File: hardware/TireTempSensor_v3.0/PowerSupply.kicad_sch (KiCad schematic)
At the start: 43 parts, among them IC3 TPS54202HDDCR, IC4 TPS54202HDDCR, Q1 FQT3P20TF, T10 TP_+5V, T11 TP_+5V, T12 TP_+5V, T13 TP_+5V, T14 TP_+3.3V, T15 TP_+2.6V, T8 TP_VCC, U2 MIC5306-2.6YD5-TR

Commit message: Piotruś prosił :3
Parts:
- removed C24, C30, C31: 22u, Capacitor_SMD:C_0805_2012Metric_Pad1.18x1.45mm_HandSolder, symbol Device:C_Small
- removed C25: 100n, Capacitor_SMD:C_0603_1608Metric_Pad1.08x0.95mm_HandSolder, symbol Device:C_Small
- removed IC3: TPS54202HDDCR, Package_TO_SOT_SMD:SOT-23-6_Handsoldering, symbol SamacsysNew:TPS54202HDDCR
- removed L3: 68u/1A4, Inductor_SMD:L_TDK_VLS6045EX_VLS6045AF, symbol Samacsys_kicad_sym:SRR4028-271Y
- removed R12: 510k, Resistor_SMD:R_0603_1608Metric_Pad0.98x0.95mm_HandSolder, symbol Device:R_Small
- removed R13: 21.8k, Resistor_SMD:R_0603_1608Metric_Pad0.98x0.95mm_HandSolder, symbol Device:R_Small
- removed T11: TP_+5V, TestPoint:TestPoint_Pad_1.0x1.0mm, symbol Connector:TestPoint_Small
- removed T8: TP_VCC, TestPoint:TestPoint_Pad_1.0x1.0mm, symbol Connector:TestPoint_Small
- added C44: 10u, Capacitor_SMD:C_0603_1608Metric_Pad1.08x0.95mm_HandSolder, symbol Device:C_Small
- added C45: 22u, Capacitor_SMD:C_0805_2012Metric_Pad1.18x1.45mm_HandSolder, symbol Device:C_Small
- added D13: +3V3, LED_SMD:LED_0603_1608Metric_Pad1.05x0.95mm_HandSolder, symbol Device:LED_Small
- added U3: LM1117-3.3, Package_TO_SOT_SMD:SOT-223-3_TabPin2, symbol Regulator_Linear:LM1117MP-3.3
- C29: value 22u -> 100n; footprint Capacitor_SMD:C_0805_2012Metric_Pad1.18x1.45mm_HandSolder -> Capacitor_SMD:C_0603_1608Metric_Pad1.08x0.95mm_HandSolder; Manufacturer_Name MCASH21GCC7684MTCA1J -> (none); Manufacturer_Part_Number CL21A107MQYNNWE -> (none); Mouser Part Number 810-C2012X5R1V226MAC -> (none); Mouser Price/Stock https://www.mouser.pl/ProductDetail/TDK/C2012X5R1V226M125AC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 -> https://www.mouser.pl/ProductDetail/Murata-Electronics/GRM0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
- R14: value 100k -> 1k; Manufacturer_Name -- -> (none); Manufacturer_Part_Number RT0603DRE07100KL -> (none); Mouser Part Number 603-RT0603DRE07100KL -> (none); Mouser Price/Stock https://www.mouser.pl/ProductDetail/KOA-Speer/RK73B1JTTD104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 -> https://www.mouser.pl/ProductDetail/Vishay-Dale/CRCW06031K0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
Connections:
- net BOOT_+3.3V is gone; now on net +5V: C27.1
- net SW_+3.3V is gone; now on net GND: C27.2
- net +5V: now also C44.1, U3.3 (VI)
- net +5V_OUT: no longer C29.1, F3.2, R14.2
- net GND: now also C44.2, C45.2, D13.1 (K), U3.1 (GND)
- net FB_+3.3V renamed VO_+3.3V
- net VO_+3.3V: now also C29.1, F3.2, C45.1, U3.2 (VO)
- new net D3V3_to_R1k: D13.2 (A), R14.2
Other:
- moved on the sheet: C14, C15, F3, F4, FB2, T14, T15, U2

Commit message: Poprawki, kontynuacja layoutu
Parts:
- Q1: footprint Mosfet:SOT-223-4-NFET -> Package_TO_SOT_SMD:SOT-223-3_TabPin2
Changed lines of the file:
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@@
 			)
 		)
-		(property "Footprint" "Mosfet:SOT-223-4-NFET"
+		(property "Footprint" "Package_TO_SOT_SMD:SOT-223-3_TabPin2"
 			(at 105.41 36.83 0)
 			(effects
@@
 			)
 		)
-		(property "Datasheet" "https://www.mouser.pl/ProductDetail/onsemi-Fairchild/FQT3P20TF?qs=k6rL%2Fc%252BPp3KKqr%252BK9hIArg%3D%3D"
+		(property "Datasheet" "https://www.mouser.pl/ProductDetail/Diodes-Incorporated/ZVP2120GTA?qs=xZ%2FP%252Ba9zWqYgxv%2FYfJ%252BkQg%3D%3D"
 			(at 107.95 41.91 0)
 			(effects

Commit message: Propozycja layoutu na spotkanie
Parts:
- removed JP1: SolderJumper_2_Open, Jumper:SolderJumper-2_P1.3mm_Open_TrianglePad1.0x1.5mm, symbol Jumper:SolderJumper_2_Open
- removed Q1: FQT3P20TF, Package_TO_SOT_SMD:SOT-223-3_TabPin2, symbol Device:Q_PMOS_DSG
- added D16: D_Schottky, Diode_SMD:D_SOD-882D, symbol Device:D_Schottky
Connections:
- net +24V safe: now also D16.1 (K)
- net at F2.2: now also D16.2 (A)
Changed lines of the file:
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@@
 	)
 	(junction
-		(at 118.11 39.37)
-		(diameter 0)
-		(color 0 0 0 0)
-	)
-	(junction
 		(at 151.13 154.305)
 		(diameter 0)
@@
 	)
 	(junction
-		(at 97.79 39.37)
-		(diameter 0)
-		(color 0 0 0 0)
-	)
-	(junction
 		(at 151.13 167.005)
 		(diameter 0)
@@
 	(wire
 		(pts
-			(xy 118.11 26.67) (xy 118.11 39.37)
-		)
-		(stroke
-			(width 0)
-			(type default)
-		)
-	)
-	(wire
-		(pts
-			(xy 111.76 26.67) (xy 118.11 26.67)
-		)
-		(stroke
-			(width 0)
-			(type default)
-		)
-	)
-	(wire
-		(pts
 			(xy 116.84 154.305) (xy 123.19 154.305)
 		)
@@
 	(wire
 		(pts
-			(xy 97.79 39.37) (xy 102.87 39.37)
+			(xy 127.635 70.485) (xy 127.635 72.39)
 		)
 		(stroke
@@
 	(wire
 		(pts
-			(xy 127.635 70.485) (xy 127.635 72.39)
+			(xy 105.41 39.37) (xy 132.715 39.37)
 		)
 		(stroke
@@
 	(wire
 		(pts
-			(xy 97.79 26.67) (xy 104.14 26.67)
-		)
-		(stroke
-			(width 0)
-			(type default)
-		)
-	)
-	(wire
-		(pts
 			(xy 60.96 164.465) (xy 60.96 167.005)
 		)
@@
 	(wire
 		(pts
-			(xy 97.79 39.37) (xy 97.79 26.67)
-		)
-		(stroke
-			(width 0)
-			(type default)
-		)
-	)
-	(wire
-		(pts
 			(xy 60.96 137.795) (xy 60.96 139.065)
 		)
@@
 	(wire
 		(pts
-			(xy 118.11 39.37) (xy 132.715 39.37)
-		)
-		(stroke
-			(width 0)
-			(type default)
-		)
-	)
-	(wire
-		(pts
 			(xy 93.98 167.005) (xy 72.39 167.005)
 		)
@@
 	(wire
 		(pts
-			(xy 113.03 39.37) (xy 118.11 39.37)
-		)
-		(stroke
-			(width 0)
-			(type default)
-		)
-	)
-	(wire
-		(pts
 			(xy 252.73 55.88) (xy 252.73 58.42)
 		)
@@
 	)
 	(symbol
+		(lib_id "Device:D_Schottky")
+		(at 101.6 39.37 180)
+		(unit 1)
+		(exclude_from_sim no)
+		(in_bom yes)
+		(on_board yes)
+		(dnp no)
+		(fields_autoplaced yes)
+		(property "Reference" "D16"
+			(at 101.9175 33.02 0)
+			(effects
+				(font
+					(size 1.27 1.27)
+				)
+			)
+		)
+		(property "Value" "D_Schottky"
+			(at 101.9175 35.56 0)
+			(effects
+				(font
+					(size 1.27 1.27)
+				)
+			)
+		)
+		(property "Footprint" "Diode_SMD:D_SOD-882D"
+			(at 101.6 39.37 0)
+			(effects
+				(font
+					(size 1.27 1.27)
+				)
+				(hide yes)
+			)
+		)
+		(property "Datasheet" "https://www.mouser.pl/ProductDetail/Nexperia/BAS70L315?qs=me8TqzrmIYUQykHMkkfEBQ%3D%3D"
+			(at 101.6 39.37 0)
+			(effects
+				(font
+					(size 1.27 1.27)
+				)
+				(hide yes)
+			)
+		)
+		(property "Description" "Schottky diode"
+			(at 101.6 39.37 0)
+			(effects
+				(font
+					(size 1.27 1.27)
+				)
+				(hide yes)
+			)
+		)
+		(pin "2"
+		)
+		(pin "1"
+		)
+		(instances
+			(project "TireTempSensor_v2.0"
+				(path "/6e95e1be-fdd6-40ae-a4f8-5c53e6058d6c/0f13de77-3258-490a-9a0b-6a199964636d"
+					(reference "D16")
+					(unit 1)
+				)
+			)
+		)
+	)
+	(symbol
 		(lib_id "Device:C_Small")
 		(at 72.39 161.925 180)
@@
 	)
 	(symbol
-		(lib_id "Device:Q_PMOS_DSG")
-		(at 107.95 41.91 90)
-		(unit 1)
-		(exclude_from_sim no)
-		(in_bom yes)
-		(on_board yes)
-		(dnp no)
-		(fields_autoplaced yes)
-		(property "Reference" "Q1"
-			(at 107.95 31.75 90)
-			(effects
-				(font
-					(size 1.27 1.27)
-				)
-			)
-		)
-		(property "Value" "FQT3P20TF"
-			(at 107.95 34.29 90)
-			(effects
-				(font
-					(size 1.27 1.27)
-				)
-			)
-		)
-		(property "Footprint" "Package_TO_SOT_SMD:SOT-223-3_TabPin2"
-			(at 105.41 36.83 0)
-			(effects
-				(font
-					(size 1.27 1.27)
-				)
-				(hide yes)
-			)
-		)
-		(property "Datasheet" "https://www.mouser.pl/ProductDetail/Diodes-Incorporated/ZVP2120GTA?qs=xZ%2FP%252Ba9zWqYgxv%2FYfJ%252BkQg%3D%3D"
-			(at 107.95 41.91 0)
-			(effects
-				(font
-					(size 1.27 1.27)
-				)
-				(hide yes)
-			)
-		)
-		(property "Description" ""
-			(at 107.95 41.91 0)
-			(effects
-				(font
-					(size 1.27 1.27)
-				)
-			)
-		)
-		(pin "1"
-		)
-		(pin "2"
-		)
-		(pin "3"
-		)
-		(instances
-			(project ""
-				(path "/6e95e1be-fdd6-40ae-a4f8-5c53e6058d6c/0f13de77-3258-490a-9a0b-6a199964636d"
-					(reference "Q1")
-					(unit 1)
-				)
-			)
-		)
-	)
-	(symbol
 		(lib_id "Device:C_Small")
 		(at 111.76 151.765 90)
@@
 	)
 	(symbol
-		(lib_id "Jumper:SolderJumper_2_Open")
-		(at 107.95 26.67 0)
-		(unit 1)
-		(exclude_from_sim no)
-		(in_bom yes)
-		(on_board yes)
-		(dnp no)
-		(fields_autoplaced yes)
-		(property "Reference" "JP1"
-			(at 107.95 20.32 0)
-			(effects
-				(font
-					(size 1.27 1.27)
-				)
-			)
-		)
-		(property "Value" "SolderJumper_2_Open"
-			(at 107.95 22.86 0)
-			(effects
-				(font
-					(size 1.27 1.27)
-				)
-			)
-		)
-		(property "Footprint" "Jumper:SolderJumper-2_P1.3mm_Open_TrianglePad1.0x1.5mm"
-			(at 107.95 26.67 0)
-			(effects
-				(font
-					(size 1.27 1.27)
-				)
-				(hide yes)
-			)
-		)
-		(property "Datasheet" "~"
-			(at 107.95 26.67 0)
-			(effects
-				(font
-					(size 1.27 1.27)
-				)
-				(hide yes)
-			)
-		)
-		(property "Description" ""
-			(at 107.95 26.67 0)
-			(effects
-				(font
-					(size 1.27 1.27)
-				)
-			)
-		)
-		(pin "1"
-		)
-		(pin "2"
-		)
-		(instances
-			(project ""
-				(path "/6e95e1be-fdd6-40ae-a4f8-5c53e6058d6c/0f13de77-3258-490a-9a0b-6a199964636d"
-					(reference "JP1")
-					(unit 1)
-				)
-			)
-		)
-	)
-	(symbol
 		(lib_id "power:PWR_FLAG")
 		(at 147.32 154.305 0)
@@
 					(unit 1)
 				)
-			)
-		)
-	)
-	(symbol
-		(lib_id "power:GND")
-		(at 107.95 46.99 0)
-		(unit 1)
-		(exclude_from_sim no)
-		(in_bom yes)
-		(on_board yes)
-		(dnp no)
-		(property "Reference" "#PWR0123"
-			(at 107.95 53.34 0)
-			(effects
-				(font
-					(size 1.27 1.27)
-				)
-				(hide yes)
-			)
-		)
-		(property "Value" "GND"
-			(at 107.95 52.07 0)
-			(effects
-				(font
-					(size 1.27 1.27)
-				)
-			)
-		)
-		(property "Footprint" ""
-			(at 107.95 46.99 0)
-			(effects
-				(font
-					(size 1.27 1.27)
-				)
-				(hide yes)
-			)
-		)
-		(property "Datasheet" ""
-			(at 107.95 46.99 0)
-			(effects
-				(font
-					(size 1.27 1.27)
-				)
-				(hide yes)
-			)
-		)
-		(property "Description" ""
-			(at 107.95 46.99 0)
-			(effects
-				(font
-					(size 1.27 1.27)
-				)
-			)
-		)
-		(pin "1"
-		)
-		(instances
-			(project ""
-				(path "/6e95e1be-fdd6-40ae-a4f8-5c53e6058d6c/0f13de77-3258-490a-9a0b-6a199964636d"
-					(reference "#PWR0123")
-					(unit 1)
-				)

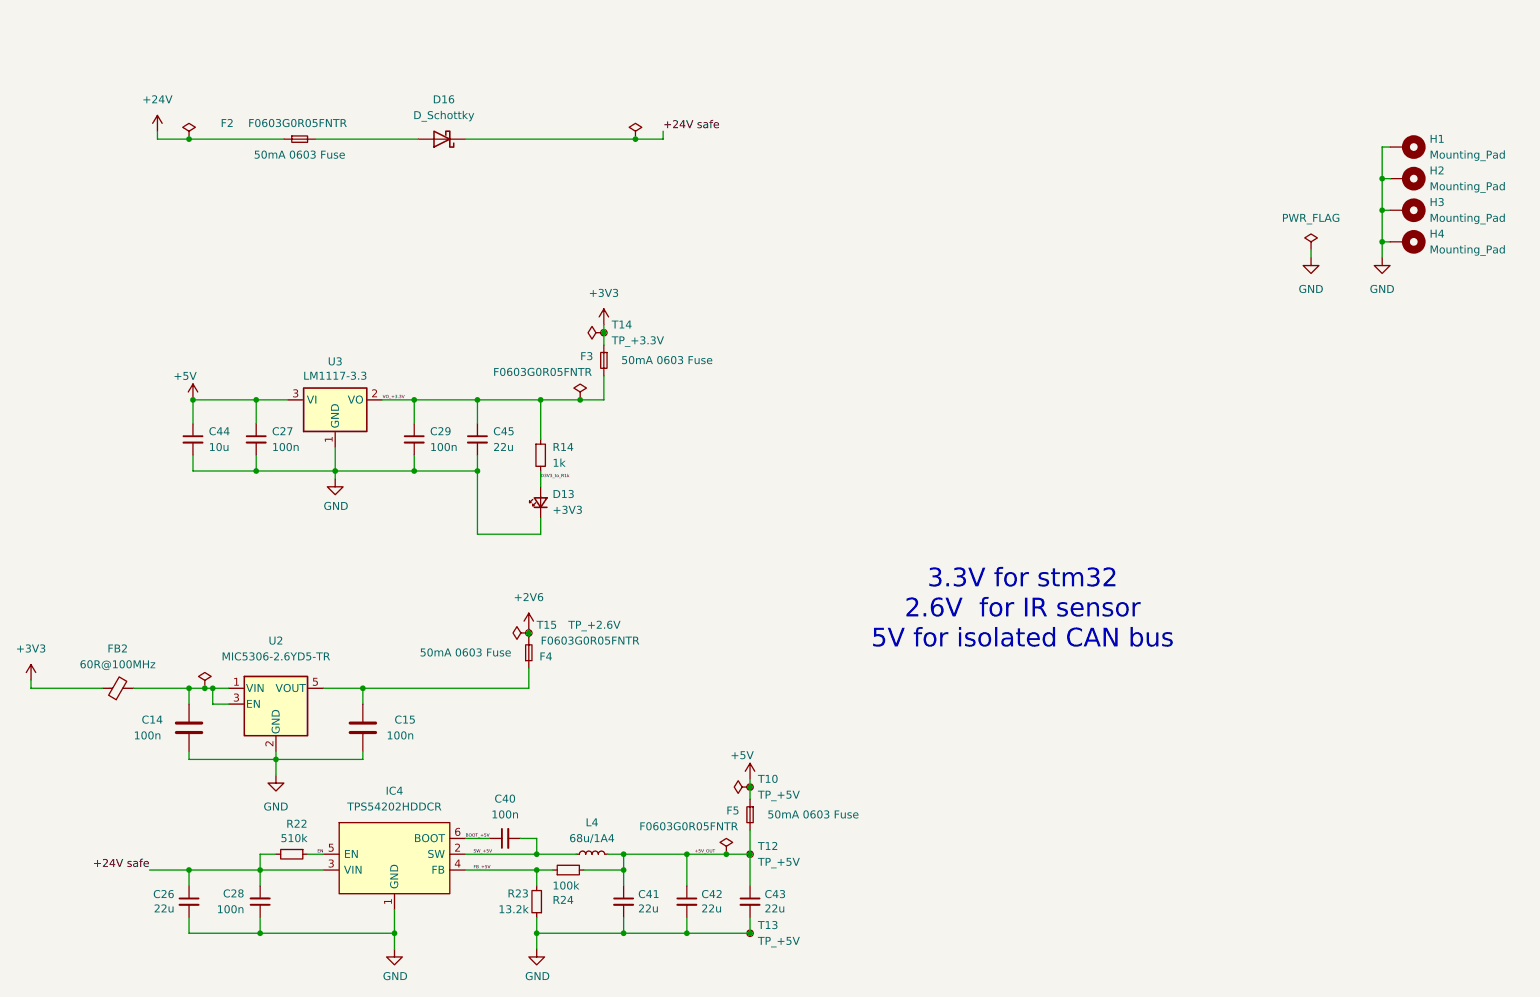
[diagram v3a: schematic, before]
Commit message: Nowy layout, nowe tvsy
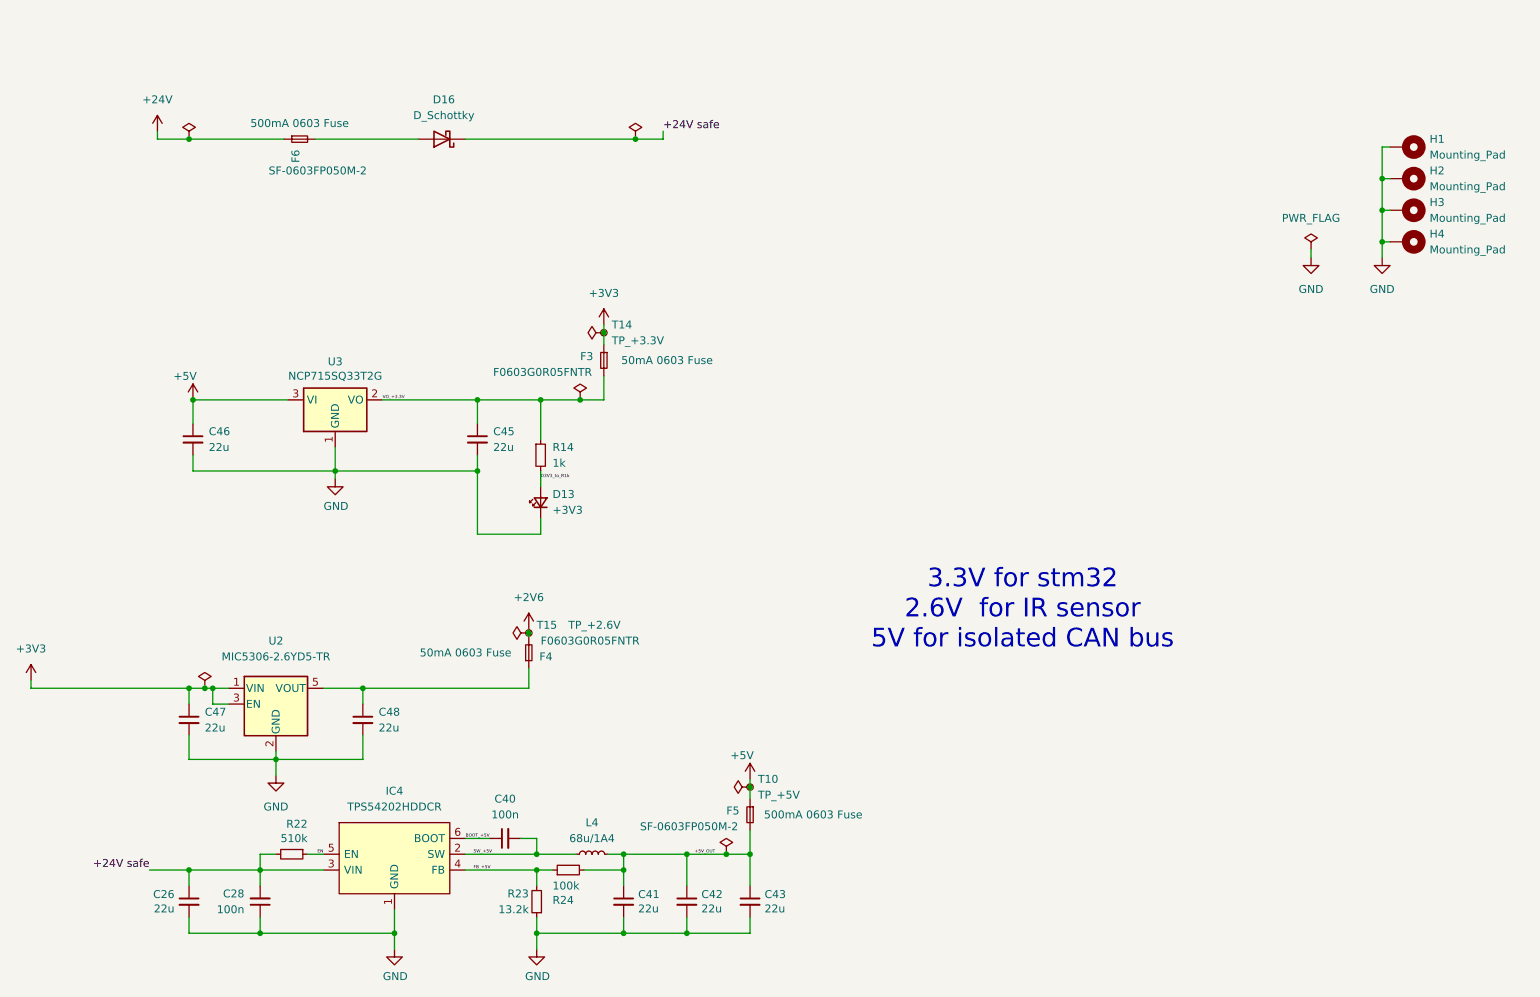
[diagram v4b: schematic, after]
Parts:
- removed C14, C15: 100n, Capacitor_SMD:C_0603_1608Metric, symbol Device:C
- removed C27, C29: 100n, Capacitor_SMD:C_0603_1608Metric_Pad1.08x0.95mm_HandSolder, symbol Device:C_Small
- removed C44: 10u, Capacitor_SMD:C_0603_1608Metric_Pad1.08x0.95mm_HandSolder, symbol Device:C_Small
- removed F2: F0603G0R05FNTR, Fuse:Fuse_0603_1608Metric_Pad1.05x0.95mm_HandSolder, symbol Device:Fuse_Small
- removed FB2: 60R@100MHz, Inductor_SMD:L_0603_1608Metric, symbol Device:FerriteBead_Small
- removed T12, T13: TP_+5V, TestPoint:TestPoint_Pad_1.0x1.0mm, symbol Connector:TestPoint_Small
- added C46, C47, C48: 22u, Capacitor_SMD:C_0805_2012Metric_Pad1.18x1.45mm_HandSolder, symbol Device:C_Small
- added F6: SF-0603FP050M-2, Fuse:Fuse_0603_1608Metric_Pad1.05x0.95mm_HandSolder, symbol Device:Fuse_Small
- F5: value F0603G0R05FNTR -> SF-0603FP050M-2
- L4: footprint Inductor_SMD:L_TDK_VLS6045EX_VLS6045AF -> Inductor_SMD:L_Vishay_IFSC-1515AH_4x4x1.8mm
- U3: value LM1117-3.3 -> NCP715SQ33T2G; footprint Package_TO_SOT_SMD:SOT-223-3_TabPin2 -> Package_TO_SOT_SMD:SOT-353_SC-70-5
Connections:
- net +24V: now also F6.1
- net +3V3: now also U2.1 (VIN), U2.3 (EN), C47.1
- net +5V: now also C46.1
- net GND: now also C46.2, C47.2, C48.2
- net at F4.1, U2.5 (VOUT): now also C48.1
- net at D16.2 (A): now also F6.2

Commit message: Poprawione :3
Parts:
- D16: footprint Diode_SMD:D_SOD-882D -> Diode_SMD:D_0603_1608Metric_Pad1.05x0.95mm_HandSolder
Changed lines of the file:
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@@
 			)
 		)
-		(property "Footprint" "Diode_SMD:D_SOD-882D"
+		(property "Footprint" "Diode_SMD:D_0603_1608Metric_Pad1.05x0.95mm_HandSolder"
 			(at 101.6 39.37 0)
 			(effects

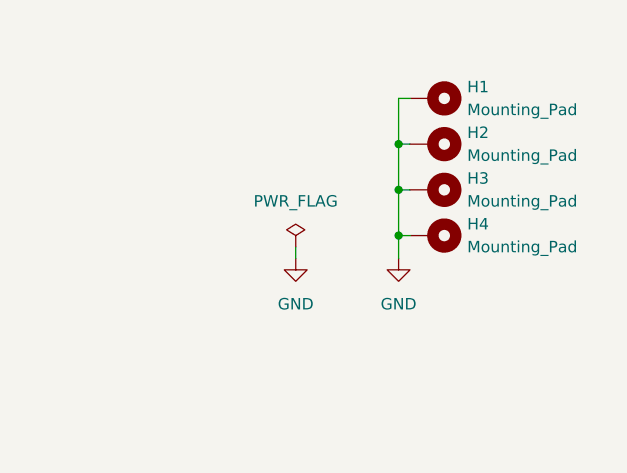
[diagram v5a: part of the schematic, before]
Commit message: Added aditional emi prevention measures
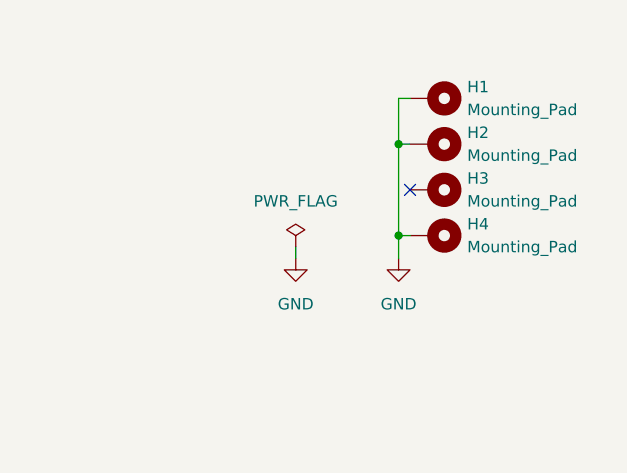
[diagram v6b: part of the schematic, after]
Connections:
- net GND: no longer H3.1
- no-connect marks 0 -> 1
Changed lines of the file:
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@@
-	)
-	(junction
-		(at 252.73 50.8)
-		(diameter 0)
-		(color 0 0 0 0)
 	)
 	(junction
@@
 		(color 0 0 0 0)
 	)
+	(no_connect
+		(at 254 50.8)
+	)
 	(wire
 		(pts
@@
 	(wire
 		(pts
-			(xy 252.73 45.72) (xy 252.73 50.8)
-		)
-		(stroke
-			(width 0)
-			(type default)
-		)
-	)
-	(wire
-		(pts
 			(xy 93.98 167.005) (xy 93.98 169.545)
 		)
@@
 	(wire
 		(pts
-			(xy 252.73 50.8) (xy 252.73 55.88)
+			(xy 252.73 45.72) (xy 252.73 55.88)
 		)
 		(stroke
@@
 		)
 		(stroke
-			(width 0)
-			(type default)
-		)
-	)
-	(wire
-		(pts
-			(xy 252.73 50.8) (xy 254 50.8)
-		)
-		(stroke

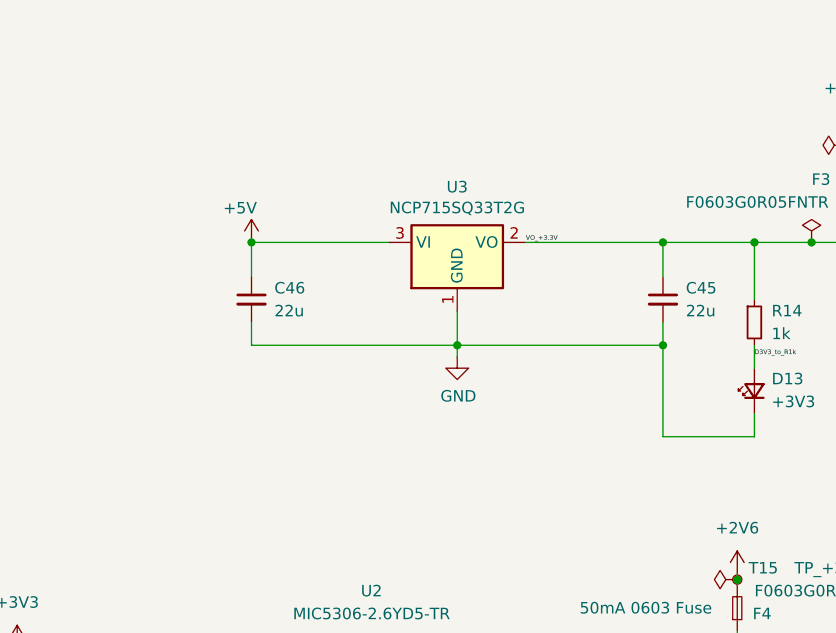
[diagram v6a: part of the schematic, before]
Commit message: Zmieniono ldo na 3.3V, dodano linki do mousera, gotowe na relase
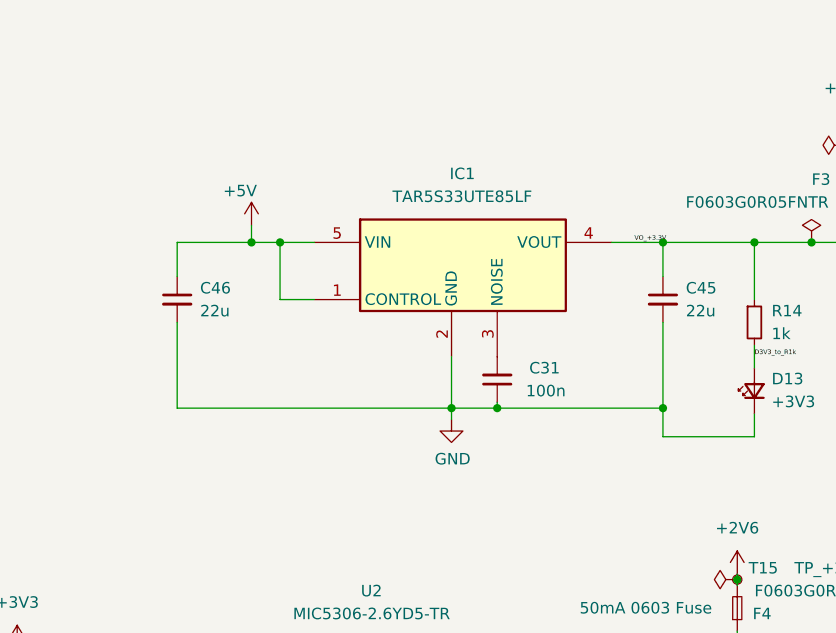
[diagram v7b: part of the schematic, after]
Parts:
- removed U3: NCP715SQ33T2G, Package_TO_SOT_SMD:SOT-353_SC-70-5, symbol Regulator_Linear:LM1117MP-3.3
- added C31: 100n, Capacitor_SMD:C_0603_1608Metric, symbol Device:C_Small
- added IC1: TAR5S33UTE85LF, footprint:SOTFL65P210X75-5N, symbol TAR5S33UTE85LF:TAR5S33UTE85LF
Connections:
- net +5V: now also IC1.1 (CONTROL), IC1.5 (VIN)
- net GND: now also C31.1, IC1.2 (GND)
- net VO_+3.3V: now also IC1.4 (VOUT)
- new net: C31.2, IC1.3 (NOISE)
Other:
- moved on the sheet: C46
